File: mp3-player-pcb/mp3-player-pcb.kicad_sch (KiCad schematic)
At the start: 39 parts, among them SW1 RotaryEncoder_Switch, SW2 Volume Up, SW3 Volume Down, U1 XIAO-ESP32-S3-Plus-SMD, U2 AO3407A, U3 MAX17048G+T10, U4 MAX98357A, U5 CR2013-MI2120

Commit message: feat: finished routing the pcb
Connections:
- net ScreenDataCommand: now also U1.1 (D0)
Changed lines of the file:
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@@
 	(global_label "ScreenDataCommand"
 		(shape input)
-		(at 68.58 43.18 180)
+		(at 69.85 43.18 180)
 		(fields_autoplaced yes)
 		(effects
@@
 		)
 		(property "Intersheetrefs" "${INTERSHEET_REFS}"
-			(at 45.638 43.18 0)
+			(at 46.908 43.18 0)
 			(hide yes)
 			(show_name no)

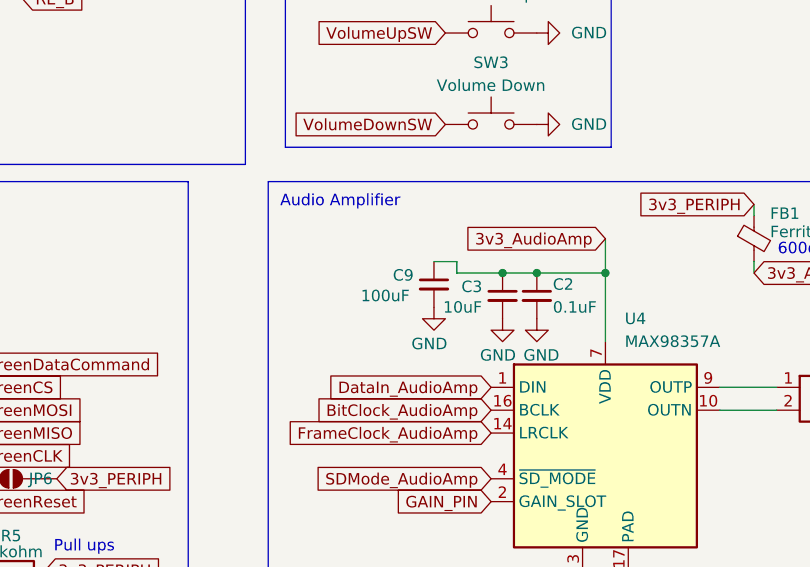
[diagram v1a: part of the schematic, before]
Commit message: bom and other parts added
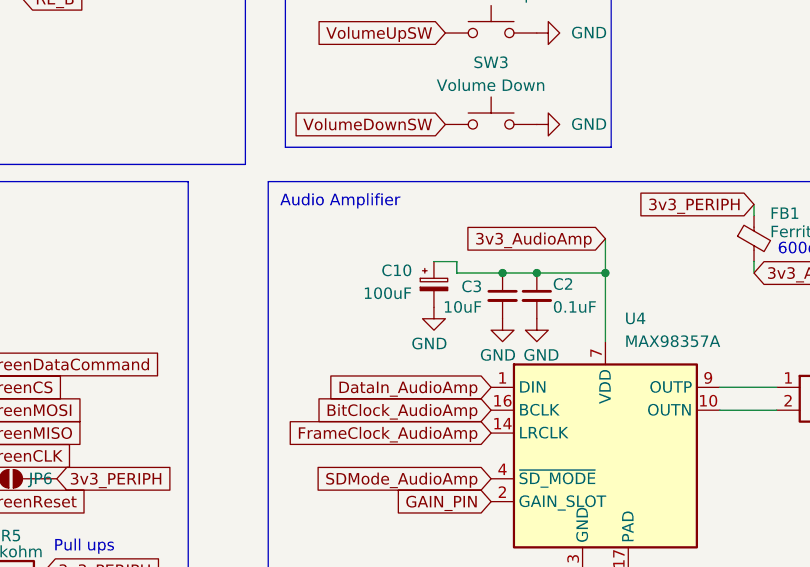
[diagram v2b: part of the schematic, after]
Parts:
- removed C9: 100uF, Capacitor_SMD:C_0603_1608Metric_Pad1.08x0.95mm_HandSolder, symbol Device:C_Small
- added C10: 100uF, Capacitor_THT:CP_Radial_D4.0mm_P2.00mm, symbol Device:C_Polarized_Small
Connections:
- net 3v3_AudioAmp: now also C10.1
- net GND: now also C10.2
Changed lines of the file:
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@@
-	)
-	(symbol
-		(lib_id "Device:C_Small")
-		(at 162.56 118.11 0)
-		(unit 1)
-		(body_style 1)
-		(exclude_from_sim no)
-		(in_bom yes)
-		(on_board yes)
-		(in_pos_files yes)
-		(dnp no)
-		(property "Reference" "C9"
-			(at 157.988 117.094 0)
-			(show_name no)
-			(do_not_autoplace no)
-			(effects
-				(font
-					(size 1.27 1.27)
-				)
-				(justify left)
-			)
-		)
-		(property "Value" "100uF"
-			(at 154.432 119.38 0)
-			(show_name no)
-			(do_not_autoplace no)
-			(effects
-				(font
-					(size 1.27 1.27)
-				)
-				(justify left)
-			)
-		)
-		(property "Footprint" "Capacitor_SMD:C_0603_1608Metric_Pad1.08x0.95mm_HandSolder"
-			(at 162.56 118.11 0)
-			(hide yes)
-			(show_name no)
-			(do_not_autoplace no)
-			(effects
-				(font
-					(size 1.27 1.27)
-				)
-			)
-		)
-		(property "Datasheet" ""
-			(at 162.56 118.11 0)
-			(hide yes)
-			(show_name no)
-			(do_not_autoplace no)
-			(effects
-				(font
-					(size 1.27 1.27)
-				)
-			)
-		)
-		(property "Description" "Unpolarized capacitor, small symbol"
-			(at 162.56 118.11 0)
-			(hide yes)
-			(show_name no)
-			(do_not_autoplace no)
-			(effects
-				(font
-					(size 1.27 1.27)
-				)
-			)
-		)
-		(pin "1"
-		)
-		(pin "2"
-		)
-		(instances
-			(project "mp3-player-pcb"
-				(path "/84bdbd45-13f3-4d12-9273-7109e21415f6"
-					(reference "C9")
-					(unit 1)
-				)
-			)
-		)
 	)
 	(symbol
@@
 					(unit 1)
 				)
+			)
+		)
+	)
+	(symbol
+		(lib_id "Device:C_Polarized_Small")
+		(at 162.56 118.11 0)
+		(unit 1)
+		(body_style 1)
+		(exclude_from_sim no)
+		(in_bom yes)
+		(on_board yes)
+		(in_pos_files yes)
+		(dnp no)
+		(property "Reference" "C10"
+			(at 156.718 116.586 0)
+			(show_name no)
+			(do_not_autoplace no)
+			(effects
+				(font
+					(size 1.27 1.27)
+				)
+				(justify left)
+			)
+		)
+		(property "Value" "100uF"
+			(at 154.686 119.126 0)
+			(show_name no)
+			(do_not_autoplace no)
+			(effects
+				(font
+					(size 1.27 1.27)
+				)
+				(justify left)
+			)
+		)
+		(property "Footprint" "Capacitor_THT:CP_Radial_D4.0mm_P2.00mm"
+			(at 162.56 118.11 0)
+			(hide yes)
+			(show_name no)
+			(do_not_autoplace no)
+			(effects
+				(font
+					(size 1.27 1.27)
+				)
+			)
+		)
+		(property "Datasheet" ""
+			(at 162.56 118.11 0)
+			(hide yes)
+			(show_name no)
+			(do_not_autoplace no)
+			(effects
+				(font
+					(size 1.27 1.27)
+				)
+			)
+		)
+		(property "Description" "Polarized capacitor, small symbol"
+			(at 162.56 118.11 0)
+			(hide yes)
+			(show_name no)
+			(do_not_autoplace no)
+			(effects
+				(font
+					(size 1.27 1.27)
+				)
+			)
+		)
+		(pin "2"
+		)
+		(pin "1"
+		)
+		(instances
+			(project "mp3-player-pcb"
+				(path "/84bdbd45-13f3-4d12-9273-7109e21415f6"
+					(reference "C10")
+					(unit 1)
+				)
